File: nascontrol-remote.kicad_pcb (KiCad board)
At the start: 2 copper layers, 50 x 90 mm, 40 parts, among them J101 Serial, J102 System IN, J103 Control, J104 System OUT, J301 USB, J302 USB_A, J303 Control USB, U101 EL817, U102 EL817, U103 EL817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

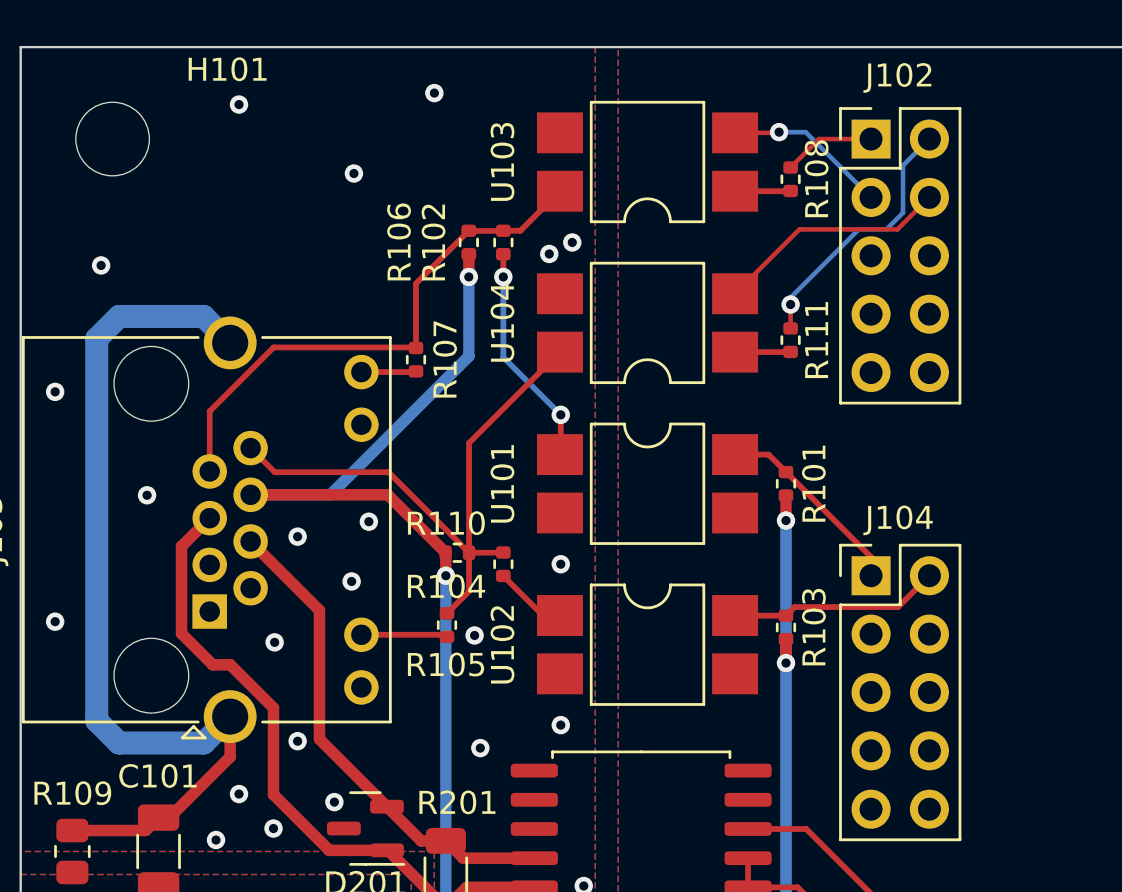
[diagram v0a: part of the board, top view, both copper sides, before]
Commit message: Fix PWR and RST issue
Signed-off-by: Benedikt Spranger <b.spranger@linutronix.de>
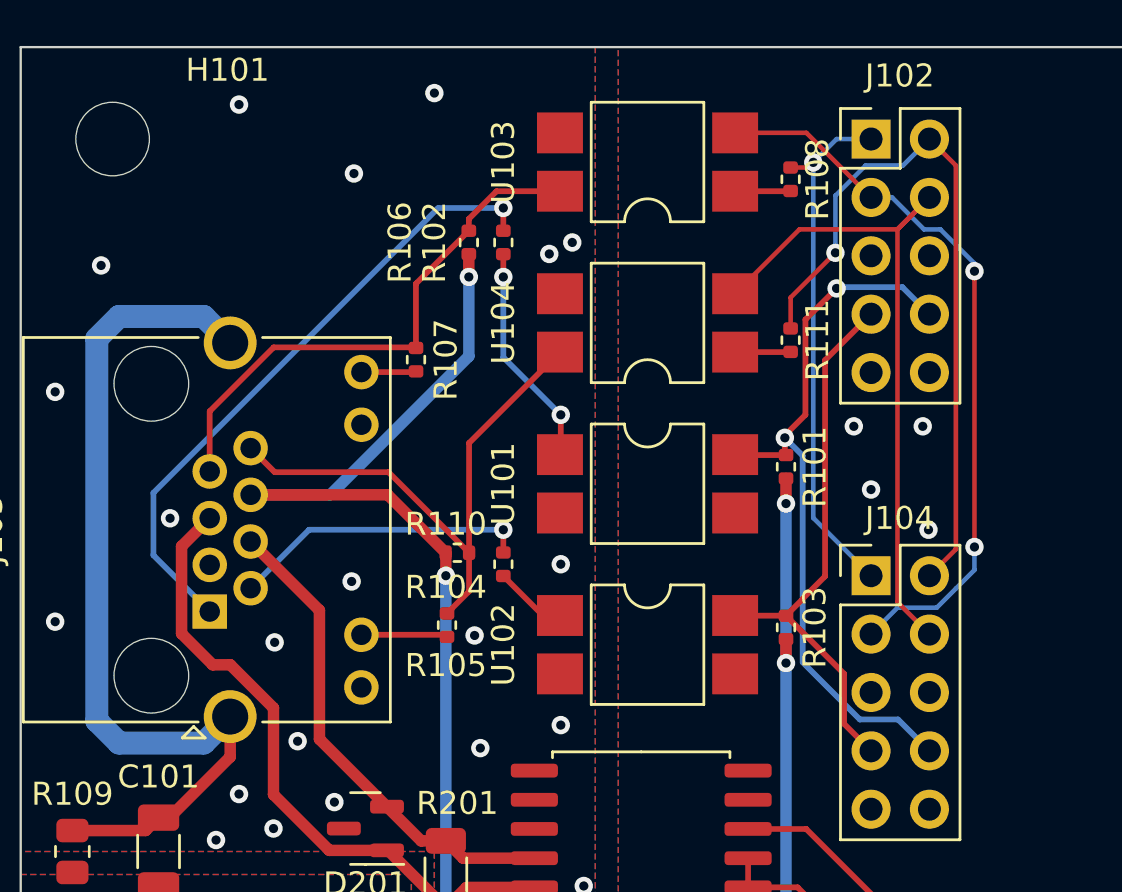
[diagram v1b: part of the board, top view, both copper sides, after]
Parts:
- moved R101 0.74 mm to (133.3, 78.3)
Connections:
- J102 pad 10: unconnected-(J102-Pad10) -> GND
- J102 pad 6: /~{PWRBTN1} -> GND
- J102 pad 7: /~{RST1} -> /~{RST2}
- J102 pad 8: GND -> /~{PWRBTN2}
- J104 pad 1: /HDLED2+ -> /HDLED1+
- J104 pad 10: unconnected-(J104-Pad10) -> GND
- J104 pad 2: /PLED2+ -> /PLED1+
- J104 pad 3: GND -> /HDLED1-
- J104 pad 4: GND -> /PLED1-
- J104 pad 6: /~{PWRBTN2} -> GND
- J104 pad 8: GND -> /~{PWRBTN2}
- R101 pad 1: /HDLED2+ -> /~{PWRBTN2}
- R102 pad 1: /HDDLED -> /PWR
- R103 pad 1: /PLED2+ -> /~{RST2}
- R104 pad 1: /PWRLED -> /RST
- U101 pad 4: /HDLED2+ -> /~{PWRBTN2}
- U102 pad 4: /PLED2+ -> /~{RST2}
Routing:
- net /~{PWRBTN2}: track 0.00 -> 32.2 mm, vias 0 -> 2
- net /PWR: track 0.00 -> 27.5 mm, vias 0 -> 1
- net /HDLED1-: track 7.09 -> 31.8 mm, vias 1 -> 2
- net /~{RST2}: track 0.00 -> 24.3 mm
- net /PLED1+: track 11.4 -> 31.6 mm
- net /PLED1-: track 10.2 -> 30.3 mm
- net /HDLED1+: track 4.01 -> 23.0 mm, vias 0 -> 1
- net /RST: track 0.00 -> 13.0 mm, vias 0 -> 1
- net /PLED2+: track 9.18 -> 0.00 mm
- net /HDLED2+: track 8.57 -> 0.00 mm
- net /PWRLED: track 26.3 -> 24.8 mm
- net +5V: track 67.4 -> 68.2 mm
- net GNDPWR: vias 24 -> 22
- net GND: vias 4 -> 8

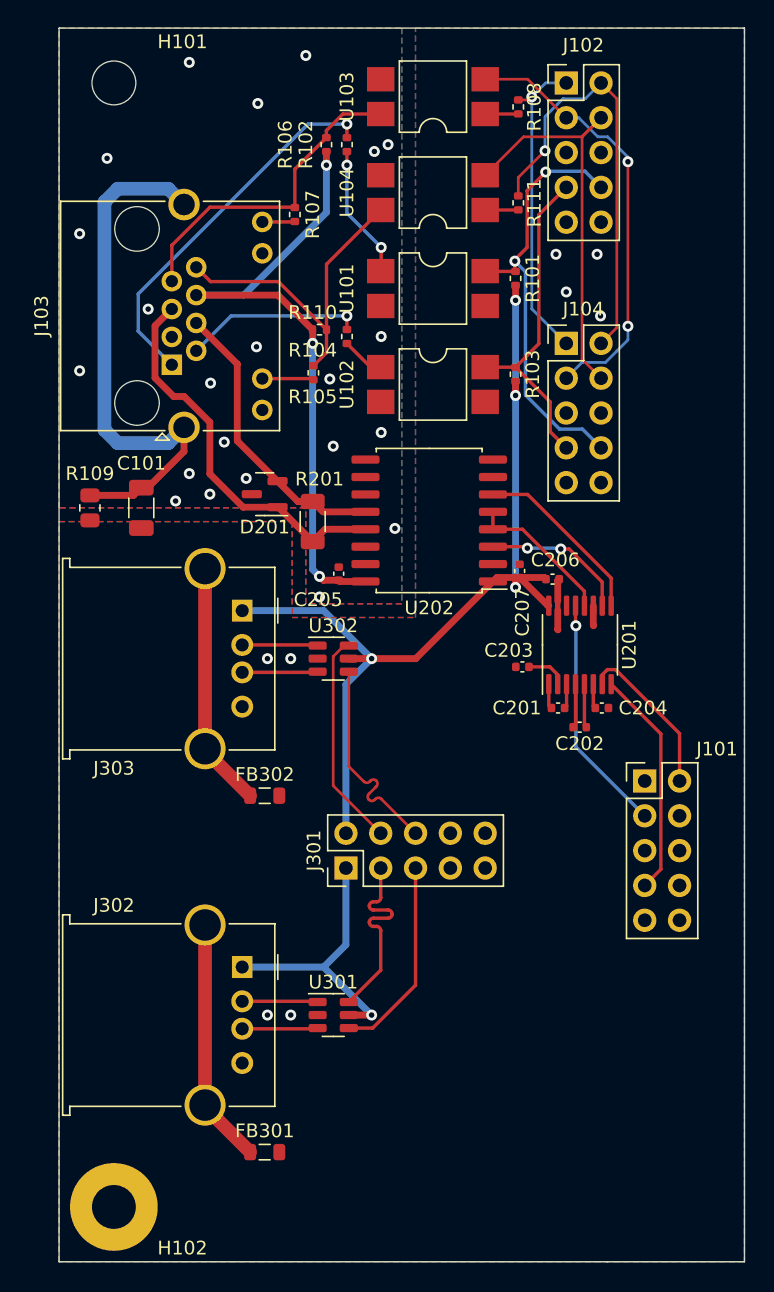
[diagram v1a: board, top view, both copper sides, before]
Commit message: Insulation cleanup
Signed-off-by: Benedikt Spranger <b.spranger@linutronix.de>
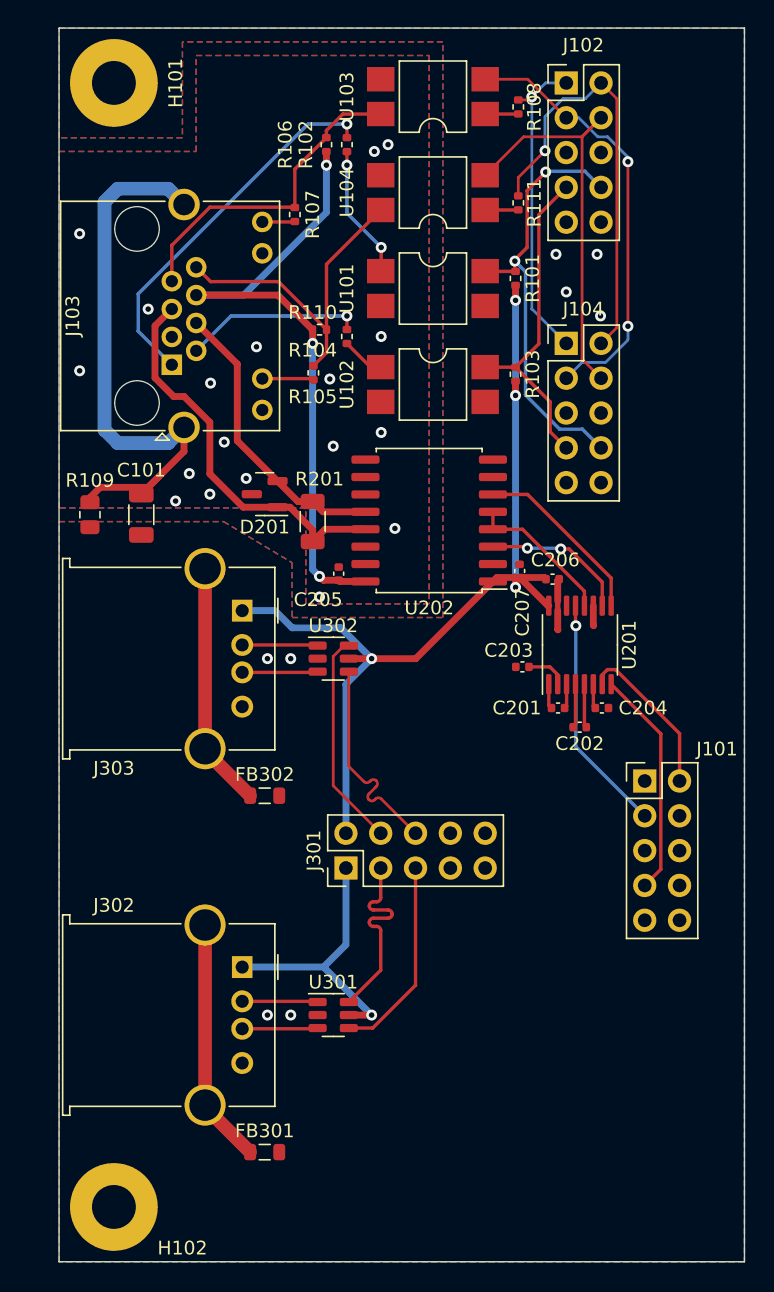
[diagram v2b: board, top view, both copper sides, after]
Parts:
- H101: footprint MountingHole:MountingHole_3.2mm_M3 -> MountingHole:MountingHole_3.2mm_M3_Pad
- moved C101 0.50 mm to (106.0, 95.5)
- moved R109 0.50 mm to (102.2, 95.5)
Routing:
- net Net-(C101-Pad1): track 39.9 -> 41.9 mm
- net /B: track 28.4 -> 28.9 mm
- net GNDPWR: vias 22 -> 18

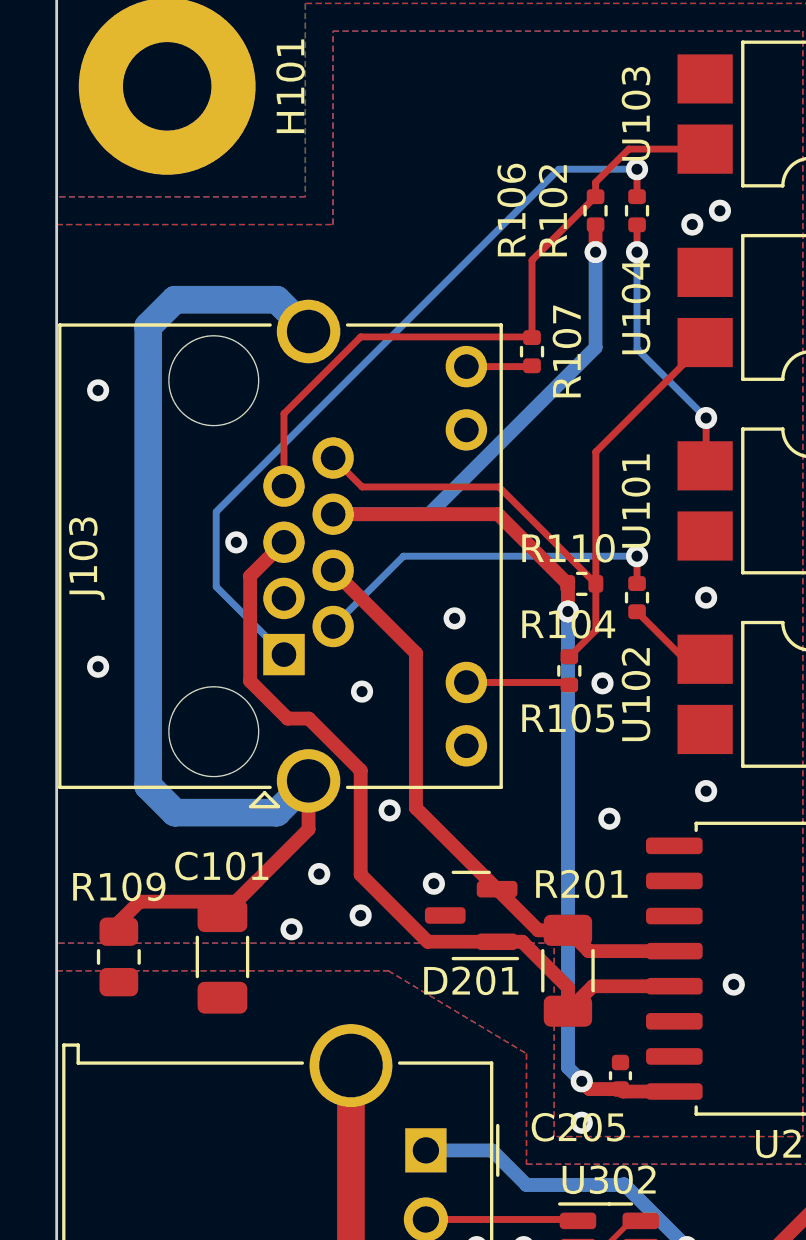
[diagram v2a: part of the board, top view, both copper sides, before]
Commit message: Inverse RJ45 connections
Signed-off-by: Benedikt Spranger <b.spranger@linutronix.de>
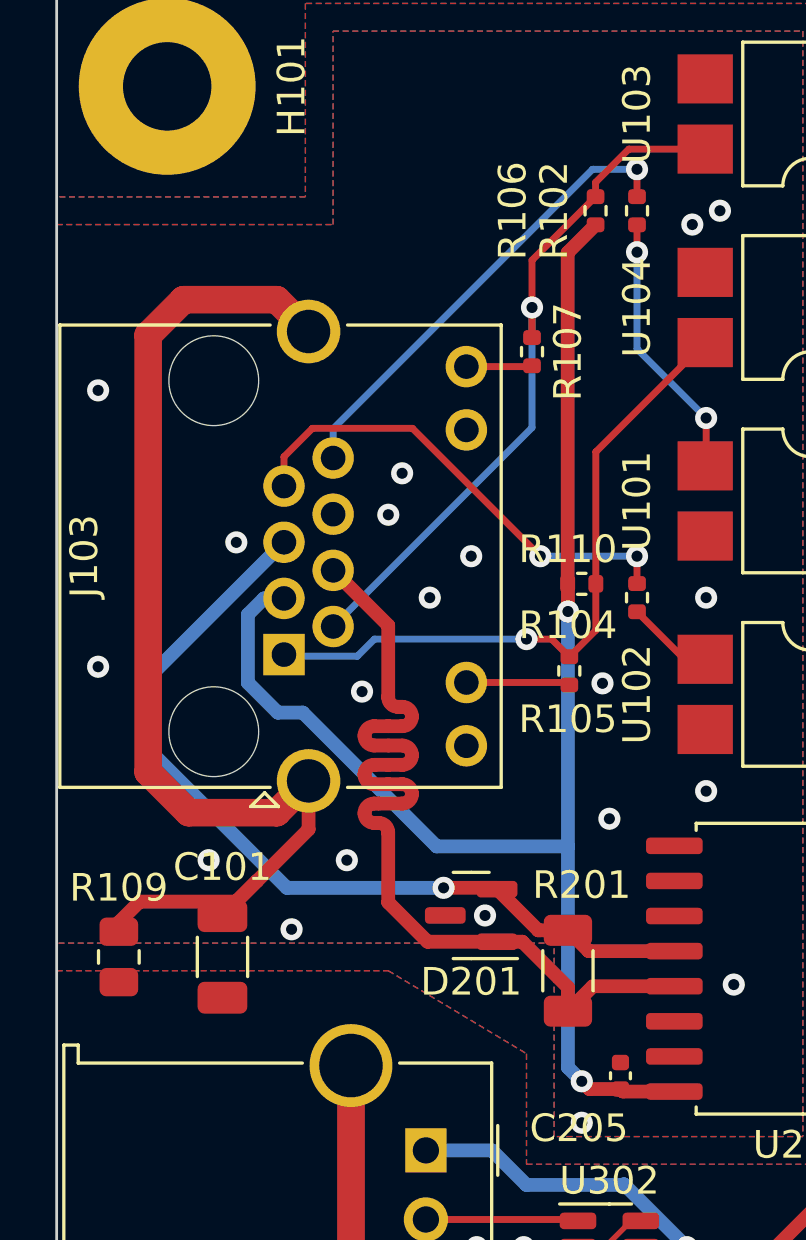
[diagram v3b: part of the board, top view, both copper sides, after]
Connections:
- J103 pad 1: /PWR -> /PWRLED
- J103 pad 2: /RST -> /HDDLED
- J103 pad 3: GNDPWR -> +3V3
- J103 pad 4: /A -> /B
- J103 pad 5: /B -> /A
- J103 pad 6: +3V3 -> GNDPWR
- J103 pad 7: /HDDLED -> /RST
- J103 pad 8: /PWRLED -> /PWR
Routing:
- net /PWR: track 27.5 -> 16.9 mm
- net /A: track 21.3 -> 31.4 mm, vias 0 -> 1
- net +3V3: track 47.7 -> 53.2 mm, vias 3 -> 2
- net /B: track 28.9 -> 33.7 mm
- net /RST: track 13.0 -> 17.2 mm, vias 1 -> 2
- net /HDDLED: track 23.8 -> 25.6 mm, vias 0 -> 1
- net /PWRLED: track 24.8 -> 24.3 mm, vias 0 -> 1
- net GNDPWR: vias 18 -> 20

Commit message: Mark PCB
Signed-off-by: Benedikt Spranger <b.spranger@linutronix.de>
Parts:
- added G***: LOGO, eurovibes:LOGO, F.Cu at (144.0, 144.0)
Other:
- board text added: "NAScontrol remote"
